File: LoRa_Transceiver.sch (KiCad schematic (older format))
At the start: 10 parts

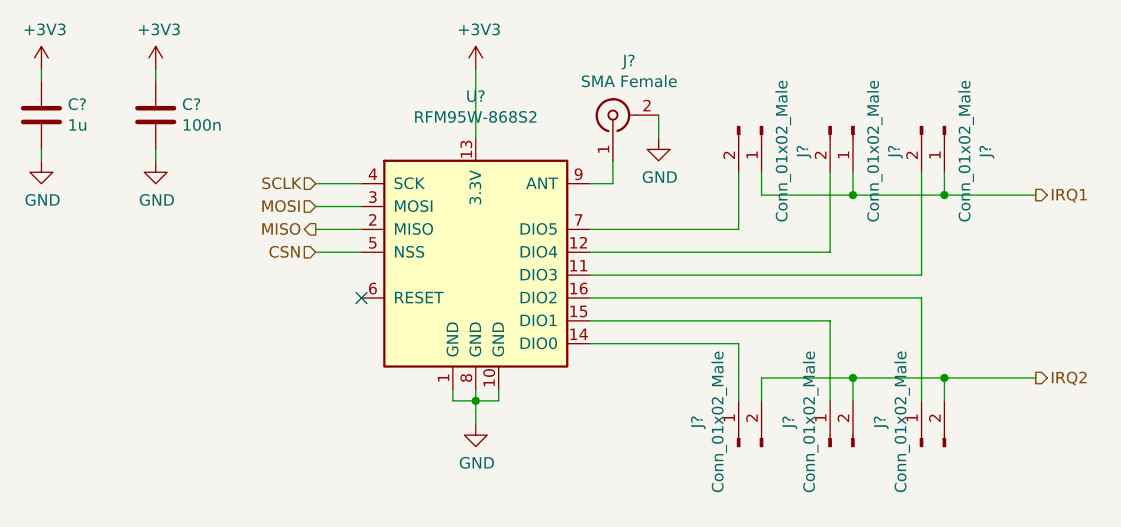
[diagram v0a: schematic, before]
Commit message: Change BME280 out for connector
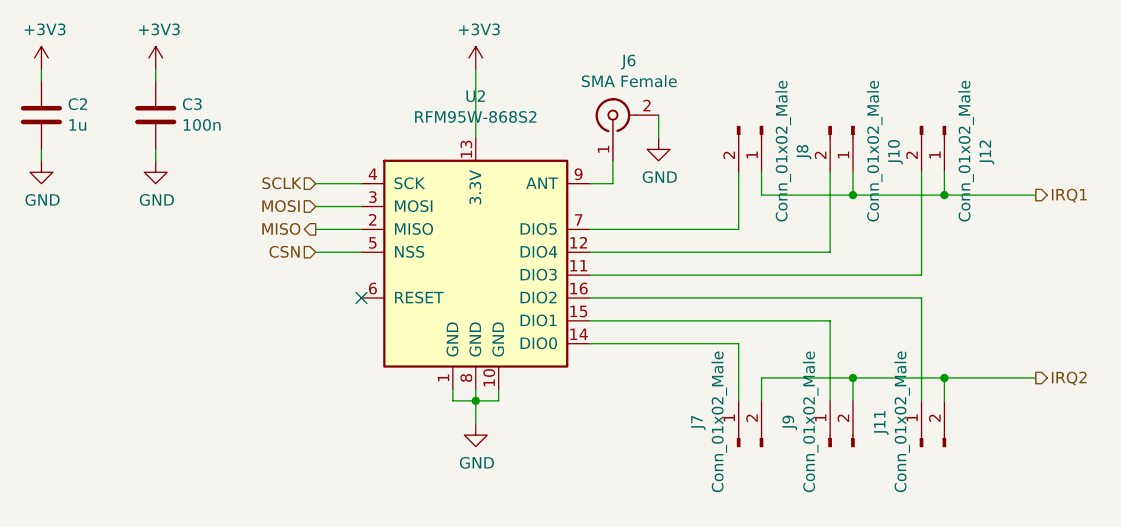
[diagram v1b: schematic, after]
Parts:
- gave numbers to parts that had none: 10
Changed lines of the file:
@@
 $EndDescr
 $Comp
-L RF_Module:RFM95W-868S2 U?
+L RF_Module:RFM95W-868S2 U2
 U 1 1 60A66EAC
 P 4400 3900
-F 0 "U?" H 4400 4581 50  0000 C CNN
+F 0 "U2" H 4400 4581 50  0000 C CNN
 F 1 "RFM95W-868S2" H 4400 4490 50  0000 C CNN
 F 2 "" H 1100 5550 50  0001 C CNN
@@
 CSN
 $Comp
-L power:+3V3 #PWR?
+L power:+3V3 #PWR022
 U 1 1 60A68377
 P 4400 3100
-F 0 "#PWR?" H 4400 2950 50  0001 C CNN
+F 0 "#PWR022" H 4400 2950 50  0001 C CNN
 F 1 "+3V3" H 4415 3273 50  0000 C CNN
 F 2 "" H 4400 3100 50  0001 C CNN
@@
 $EndComp
 $Comp
-L power:GND #PWR?
+L power:GND #PWR023
 U 1 1 60A684F7
 P 4400 4650
-F 0 "#PWR?" H 4400 4400 50  0001 C CNN
+F 0 "#PWR023" H 4400 4400 50  0001 C CNN
 F 1 "GND" H 4405 4477 50  0000 C CNN
 F 2 "" H 4400 4650 50  0001 C CNN
@@
 	5000 3600 5000 3500
 $Comp
-L Connector:Conn_01x02_Male J?
+L Connector:Conn_01x02_Male J8
 U 1 1 60A6BDC1
 P 5650 3350
-F 0 "J?" H 5758 3531 50  0000 C CNN
+F 0 "J8" H 5758 3531 50  0000 C CNN
 F 1 "Conn_01x02_Male" H 5758 3440 50  0000 C CNN
 F 2 "" H 5650 3350 50  0001 C CNN
@@
 $EndComp
 $Comp
-L Connector:Conn_01x02_Male J?
+L Connector:Conn_01x02_Male J10
 U 1 1 60A6C78E
 P 6050 3350
-F 0 "J?" H 6158 3531 50  0000 C CNN
+F 0 "J10" H 6158 3531 50  0000 C CNN
 F 1 "Conn_01x02_Male" H 6158 3440 50  0000 C CNN
 F 2 "" H 6050 3350 50  0001 C CNN
@@
 $EndComp
 $Comp
-L Connector:Conn_01x02_Male J?
+L Connector:Conn_01x02_Male J7
 U 1 1 60A6C92B
 P 5550 4750
-F 0 "J?" H 5658 4931 50  0000 C CNN
+F 0 "J7" H 5658 4931 50  0000 C CNN
 F 1 "Conn_01x02_Male" H 5658 4840 50  0000 C CNN
 F 2 "" H 5550 4750 50  0001 C CNN
@@
 $EndComp
 $Comp
-L Connector:Conn_01x02_Male J?
+L Connector:Conn_01x02_Male J9
 U 1 1 60A6CADE
 P 5950 4750
-F 0 "J?" H 6058 4931 50  0000 C CNN
+F 0 "J9" H 6058 4931 50  0000 C CNN
 F 1 "Conn_01x02_Male" H 6058 4840 50  0000 C CNN
 F 2 "" H 5950 4750 50  0001 C CNN
@@
 $EndComp
 $Comp
-L Connector:Conn_01x02_Male J?
+L Connector:Conn_01x02_Male J12
 U 1 1 60A6CCA7
 P 6450 3350
-F 0 "J?" H 6558 3531 50  0000 C CNN
+F 0 "J12" H 6558 3531 50  0000 C CNN
 F 1 "Conn_01x02_Male" H 6558 3440 50  0000 C CNN
 F 2 "" H 6450 3350 50  0001 C CNN
@@
 $EndComp
 $Comp
-L Connector:Conn_01x02_Male J?
+L Connector:Conn_01x02_Male J11
 U 1 1 60A6CE81
 P 6350 4750
-F 0 "J?" H 6458 4931 50  0000 C CNN
+F 0 "J11" H 6458 4931 50  0000 C CNN
 F 1 "Conn_01x02_Male" H 6458 4840 50  0000 C CNN
 F 2 "" H 6350 4750 50  0001 C CNN
@@
 	4900 4200 5950 4200
 $Comp
-L power:+3V3 #PWR?
+L power:+3V3 #PWR020
 U 1 1 60A81EA0
 P 3000 3100
-F 0 "#PWR?" H 3000 2950 50  0001 C CNN
+F 0 "#PWR020" H 3000 2950 50  0001 C CNN
 F 1 "+3V3" H 3015 3273 50  0000 C CNN
 F 2 "" H 3000 3100 50  0001 C CNN
@@
 $EndComp
 $Comp
-L power:GND #PWR?
+L power:GND #PWR021
 U 1 1 60A83B85
 P 3000 3500
-F 0 "#PWR?" H 3000 3250 50  0001 C CNN
+F 0 "#PWR021" H 3000 3250 50  0001 C CNN
 F 1 "GND" H 3005 3327 50  0000 C CNN
 F 2 "" H 3000 3500 50  0001 C CNN
@@
 $EndComp
 $Comp
-L Device:C C?
+L Device:C C3
 U 1 1 60A845BF
 P 3000 3300
-F 0 "C?" H 3115 3346 50  0000 L CNN
+F 0 "C3" H 3115 3346 50  0000 L CNN
 F 1 "100n" H 3115 3255 50  0000 L CNN
 F 2 "" H 3038 3150 50  0001 C CNN
@@
 	3000 3150 3000 3100
 $Comp
-L power:GND #PWR?
+L power:GND #PWR019
 U 1 1 60A85D82
 P 2500 3500
-F 0 "#PWR?" H 2500 3250 50  0001 C CNN
+F 0 "#PWR019" H 2500 3250 50  0001 C CNN
 F 1 "GND" H 2505 3327 50  0000 C CNN
 F 2 "" H 2500 3500 50  0001 C CNN
@@
 $EndComp
 $Comp
-L power:+3V3 #PWR?
+L power:+3V3 #PWR018
 U 1 1 60A86C18
 P 2500 3100
-F 0 "#PWR?" H 2500 2950 50  0001 C CNN
+F 0 "#PWR018" H 2500 2950 50  0001 C CNN
 F 1 "+3V3" H 2515 3273 50  0000 C CNN
 F 2 "" H 2500 3100 50  0001 C CNN
@@
 $EndComp
 $Comp
-L Device:C C?
+L Device:C C2
 U 1 1 60A882A8
 P 2500 3300
-F 0 "C?" H 2615 3346 50  0000 L CNN
+F 0 "C2" H 2615 3346 50  0000 L CNN
 F 1 "1u" H 2615 3255 50  0000 L CNN
 F 2 "" H 2538 3150 50  0001 C CNN
@@
 	2500 3150 2500 3100
 $Comp
-L Connector:Conn_Coaxial J?
+L Connector:Conn_Coaxial J6
 U 1 1 60A7FEF3
 P 5000 3300
-F 0 "J?" V 5237 3229 50  0000 C CNN
+F 0 "J6" V 5237 3229 50  0000 C CNN
 F 1 "SMA Female" V 5146 3229 50  0000 C CNN
 F 2 "" H 5000 3300 50  0001 C CNN
@@
 $EndComp
 $Comp
-L power:GND #PWR?
+L power:GND #PWR024
 U 1 1 60A8218B
 P 5200 3400
-F 0 "#PWR?" H 5200 3150 50  0001 C CNN
+F 0 "#PWR024" H 5200 3150 50  0001 C CNN
 F 1 "GND" H 5205 3227 50  0000 C CNN
 F 2 "" H 5200 3400 50  0001 C CNN

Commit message: Begin assigning footprints
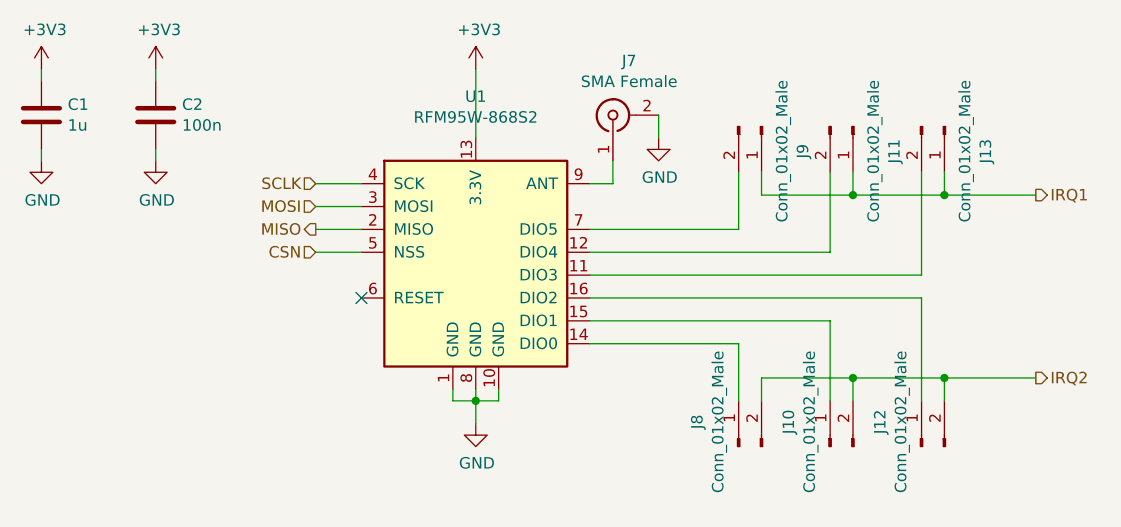
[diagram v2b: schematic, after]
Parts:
- C1: renamed from C2; footprint (none) -> Capacitor_SMD:C_0603_1608Metric; LCSC (none) -> C15849
- C2: renamed from C3; footprint (none) -> Capacitor_SMD:C_0603_1608Metric; LCSC (none) -> C14663
- J10: renamed from J9; footprint (none) -> Connector_PinHeader_2.54mm:PinHeader_1x02_P2.54mm_Vertical
- J11: renamed from J10; footprint (none) -> Connector_PinHeader_2.54mm:PinHeader_1x02_P2.54mm_Vertical
- J12: renamed from J11; footprint (none) -> Connector_PinHeader_2.54mm:PinHeader_1x02_P2.54mm_Vertical
- J13: renamed from J12; footprint (none) -> Connector_PinHeader_2.54mm:PinHeader_1x02_P2.54mm_Vertical
- J8: renamed from J7; footprint (none) -> Connector_PinHeader_2.54mm:PinHeader_1x02_P2.54mm_Vertical
- J9: renamed from J8; footprint (none) -> Connector_PinHeader_2.54mm:PinHeader_1x02_P2.54mm_Vertical
- renumbered J6 to J7, U2 to U1
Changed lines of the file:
@@
 $EndDescr
 $Comp
-L RF_Module:RFM95W-868S2 U2
+L RF_Module:RFM95W-868S2 U1
 U 1 1 60A66EAC
 P 4400 3900
-F 0 "U2" H 4400 4581 50  0000 C CNN
+F 0 "U1" H 4400 4581 50  0000 C CNN
 F 1 "RFM95W-868S2" H 4400 4490 50  0000 C CNN
 F 2 "" H 1100 5550 50  0001 C CNN
@@
 CSN
 $Comp
-L power:+3V3 #PWR022
+L power:+3V3 #PWR020
 U 1 1 60A68377
 P 4400 3100
-F 0 "#PWR022" H 4400 2950 50  0001 C CNN
+F 0 "#PWR020" H 4400 2950 50  0001 C CNN
 F 1 "+3V3" H 4415 3273 50  0000 C CNN
 F 2 "" H 4400 3100 50  0001 C CNN
@@
 $EndComp
 $Comp
-L power:GND #PWR023
+L power:GND #PWR021
 U 1 1 60A684F7
 P 4400 4650
-F 0 "#PWR023" H 4400 4400 50  0001 C CNN
+F 0 "#PWR021" H 4400 4400 50  0001 C CNN
 F 1 "GND" H 4405 4477 50  0000 C CNN
 F 2 "" H 4400 4650 50  0001 C CNN
@@
 	5000 3600 5000 3500
 $Comp
-L Connector:Conn_01x02_Male J8
+L Connector:Conn_01x02_Male J9
 U 1 1 60A6BDC1
 P 5650 3350
-F 0 "J8" H 5758 3531 50  0000 C CNN
+F 0 "J9" H 5758 3531 50  0000 C CNN
 F 1 "Conn_01x02_Male" H 5758 3440 50  0000 C CNN
-F 2 "" H 5650 3350 50  0001 C CNN
+F 2 "Connector_PinHeader_2.54mm:PinHeader_1x02_P2.54mm_Vertical" H 5650 3350 50  0001 C CNN
 F 3 "~" H 5650 3350 50  0001 C CNN
 	1    5650 3350
@@
 $EndComp
 $Comp
-L Connector:Conn_01x02_Male J10
+L Connector:Conn_01x02_Male J11
 U 1 1 60A6C78E
 P 6050 3350
-F 0 "J10" H 6158 3531 50  0000 C CNN
+F 0 "J11" H 6158 3531 50  0000 C CNN
 F 1 "Conn_01x02_Male" H 6158 3440 50  0000 C CNN
-F 2 "" H 6050 3350 50  0001 C CNN
+F 2 "Connector_PinHeader_2.54mm:PinHeader_1x02_P2.54mm_Vertical" H 6050 3350 50  0001 C CNN
 F 3 "~" H 6050 3350 50  0001 C CNN
 	1    6050 3350
@@
 $EndComp
 $Comp
-L Connector:Conn_01x02_Male J7
+L Connector:Conn_01x02_Male J8
 U 1 1 60A6C92B
 P 5550 4750
-F 0 "J7" H 5658 4931 50  0000 C CNN
+F 0 "J8" H 5658 4931 50  0000 C CNN
 F 1 "Conn_01x02_Male" H 5658 4840 50  0000 C CNN
-F 2 "" H 5550 4750 50  0001 C CNN
+F 2 "Connector_PinHeader_2.54mm:PinHeader_1x02_P2.54mm_Vertical" H 5550 4750 50  0001 C CNN
 F 3 "~" H 5550 4750 50  0001 C CNN
 	1    5550 4750
@@
 $EndComp
 $Comp
-L Connector:Conn_01x02_Male J9
+L Connector:Conn_01x02_Male J10
 U 1 1 60A6CADE
 P 5950 4750
-F 0 "J9" H 6058 4931 50  0000 C CNN
+F 0 "J10" H 6058 4931 50  0000 C CNN
 F 1 "Conn_01x02_Male" H 6058 4840 50  0000 C CNN
-F 2 "" H 5950 4750 50  0001 C CNN
+F 2 "Connector_PinHeader_2.54mm:PinHeader_1x02_P2.54mm_Vertical" H 5950 4750 50  0001 C CNN
 F 3 "~" H 5950 4750 50  0001 C CNN
 	1    5950 4750
@@
 $EndComp
 $Comp
-L Connector:Conn_01x02_Male J12
+L Connector:Conn_01x02_Male J13
 U 1 1 60A6CCA7
 P 6450 3350
-F 0 "J12" H 6558 3531 50  0000 C CNN
+F 0 "J13" H 6558 3531 50  0000 C CNN
 F 1 "Conn_01x02_Male" H 6558 3440 50  0000 C CNN
-F 2 "" H 6450 3350 50  0001 C CNN
+F 2 "Connector_PinHeader_2.54mm:PinHeader_1x02_P2.54mm_Vertical" H 6450 3350 50  0001 C CNN
 F 3 "~" H 6450 3350 50  0001 C CNN
 	1    6450 3350
@@
 $EndComp
 $Comp
-L Connector:Conn_01x02_Male J11
+L Connector:Conn_01x02_Male J12
 U 1 1 60A6CE81
 P 6350 4750
-F 0 "J11" H 6458 4931 50  0000 C CNN
+F 0 "J12" H 6458 4931 50  0000 C CNN
 F 1 "Conn_01x02_Male" H 6458 4840 50  0000 C CNN
-F 2 "" H 6350 4750 50  0001 C CNN
+F 2 "Connector_PinHeader_2.54mm:PinHeader_1x02_P2.54mm_Vertical" H 6350 4750 50  0001 C CNN
 F 3 "~" H 6350 4750 50  0001 C CNN
 	1    6350 4750
@@
 	4900 4200 5950 4200
 $Comp
-L power:+3V3 #PWR020
+L power:+3V3 #PWR018
 U 1 1 60A81EA0
 P 3000 3100
-F 0 "#PWR020" H 3000 2950 50  0001 C CNN
+F 0 "#PWR018" H 3000 2950 50  0001 C CNN
 F 1 "+3V3" H 3015 3273 50  0000 C CNN
 F 2 "" H 3000 3100 50  0001 C CNN
@@
 $EndComp
 $Comp
-L power:GND #PWR021
+L power:GND #PWR019
 U 1 1 60A83B85
 P 3000 3500
-F 0 "#PWR021" H 3000 3250 50  0001 C CNN
+F 0 "#PWR019" H 3000 3250 50  0001 C CNN
 F 1 "GND" H 3005 3327 50  0000 C CNN
 F 2 "" H 3000 3500 50  0001 C CNN
@@
 $EndComp
 $Comp
-L Device:C C3
+L Device:C C2
 U 1 1 60A845BF
 P 3000 3300
-F 0 "C3" H 3115 3346 50  0000 L CNN
+F 0 "C2" H 3115 3346 50  0000 L CNN
 F 1 "100n" H 3115 3255 50  0000 L CNN
-F 2 "" H 3038 3150 50  0001 C CNN
+F 2 "Capacitor_SMD:C_0603_1608Metric" H 3038 3150 50  0001 C CNN
 F 3 "~" H 3000 3300 50  0001 C CNN
+F 4 "C14663" H 3000 3300 50  0001 C CNN "LCSC"
 	1    3000 3300
 	1    0    0    -1
@@
 	3000 3150 3000 3100
 $Comp
-L power:GND #PWR019
+L power:GND #PWR017
 U 1 1 60A85D82
 P 2500 3500
-F 0 "#PWR019" H 2500 3250 50  0001 C CNN
+F 0 "#PWR017" H 2500 3250 50  0001 C CNN
 F 1 "GND" H 2505 3327 50  0000 C CNN
 F 2 "" H 2500 3500 50  0001 C CNN
@@
 $EndComp
 $Comp
-L power:+3V3 #PWR018
+L power:+3V3 #PWR016
 U 1 1 60A86C18
 P 2500 3100
-F 0 "#PWR018" H 2500 2950 50  0001 C CNN
+F 0 "#PWR016" H 2500 2950 50  0001 C CNN
 F 1 "+3V3" H 2515 3273 50  0000 C CNN
 F 2 "" H 2500 3100 50  0001 C CNN
@@
 $EndComp
 $Comp
-L Device:C C2
+L Device:C C1
 U 1 1 60A882A8
 P 2500 3300
-F 0 "C2" H 2615 3346 50  0000 L CNN
+F 0 "C1" H 2615 3346 50  0000 L CNN
 F 1 "1u" H 2615 3255 50  0000 L CNN
-F 2 "" H 2538 3150 50  0001 C CNN
+F 2 "Capacitor_SMD:C_0603_1608Metric" H 2538 3150 50  0001 C CNN
 F 3 "~" H 2500 3300 50  0001 C CNN
+F 4 "C15849" H 2500 3300 50  0001 C CNN "LCSC"
 	1    2500 3300
 	1    0    0    -1
@@
 	2500 3150 2500 3100
 $Comp
-L Connector:Conn_Coaxial J6
+L Connector:Conn_Coaxial J7
 U 1 1 60A7FEF3
 P 5000 3300
-F 0 "J6" V 5237 3229 50  0000 C CNN
+F 0 "J7" V 5237 3229 50  0000 C CNN
 F 1 "SMA Female" V 5146 3229 50  0000 C CNN
 F 2 "" H 5000 3300 50  0001 C CNN
@@
 $EndComp
 $Comp
-L power:GND #PWR024
+L power:GND #PWR022
 U 1 1 60A8218B
 P 5200 3400
-F 0 "#PWR024" H 5200 3150 50  0001 C CNN
+F 0 "#PWR022" H 5200 3150 50  0001 C CNN
 F 1 "GND" H 5205 3227 50  0000 C CNN
 F 2 "" H 5200 3400 50  0001 C CNN

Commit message: Finish attaching footprints for revision 1
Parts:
- J7: footprint (none) -> co2_sensor_node:TE_5-1814832-2_C482015
- U1: footprint (none) -> RF_Module:HOPERF_RFM9XW_SMD
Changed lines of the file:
@@
 F 0 "U1" H 4400 4581 50  0000 C CNN
 F 1 "RFM95W-868S2" H 4400 4490 50  0000 C CNN
-F 2 "" H 1100 5550 50  0001 C CNN
+F 2 "RF_Module:HOPERF_RFM9XW_SMD" H 1100 5550 50  0001 C CNN
 F 3 "https://www.hoperf.com/data/upload/portal/20181127/5bfcbea20e9ef.pdf" H 1100 5550 50  0001 C CNN
 	1    4400 3900
@@
 F 0 "J7" V 5237 3229 50  0000 C CNN
 F 1 "SMA Female" V 5146 3229 50  0000 C CNN
-F 2 "" H 5000 3300 50  0001 C CNN
+F 2 "co2_sensor_node:TE_5-1814832-2_C482015" H 5000 3300 50  0001 C CNN
 F 3 " ~" H 5000 3300 50  0001 C CNN
 	1    5000 3300

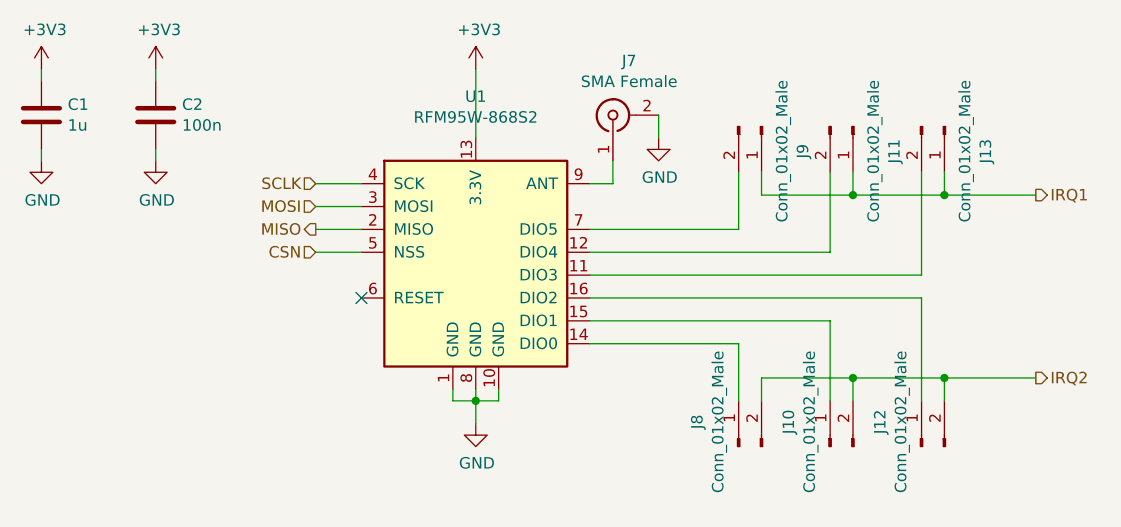
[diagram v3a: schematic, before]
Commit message: First cut at layout
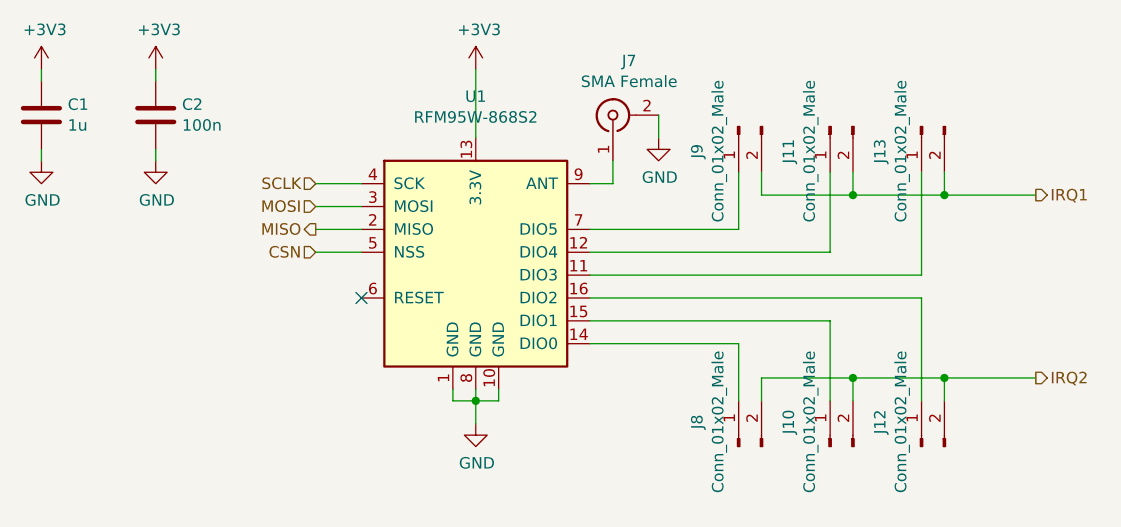
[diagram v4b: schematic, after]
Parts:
- J10, J11, J12, J13, J8, J9: footprint Connector_PinHeader_2.54mm:PinHeader_1x02_P2.54mm_Vertical -> Jumper:SolderJumper-2_P1.3mm_Open_TrianglePad1.0x1.5mm
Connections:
- net IRQ1: now also J11.2 (Pin_2), J13.2 (Pin_2), J9.2 (Pin_2); no longer J11.1 (Pin_1), J13.1 (Pin_1), J9.1 (Pin_1)
- net at U1.11 (DIO3): now also J13.1 (Pin_1); no longer J13.2 (Pin_2)
- net at U1.12 (DIO4): now also J11.1 (Pin_1); no longer J11.2 (Pin_2)
- net at U1.7 (DIO5): now also J9.1 (Pin_1); no longer J9.2 (Pin_2)
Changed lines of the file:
@@
 L Connector:Conn_01x02_Male J9
 U 1 1 60A6BDC1
-P 5650 3350
-F 0 "J9" H 5758 3531 50  0000 C CNN
-F 1 "Conn_01x02_Male" H 5758 3440 50  0000 C CNN
-F 2 "Connector_PinHeader_2.54mm:PinHeader_1x02_P2.54mm_Vertical" H 5650 3350 50  0001 C CNN
-F 3 "~" H 5650 3350 50  0001 C CNN
-	1    5650 3350
-	0    1    1    0
+P 5550 3350
+F 0 "J9" H 5658 3531 50  0000 C CNN
+F 1 "Conn_01x02_Male" H 5658 3440 50  0000 C CNN
+F 2 "Jumper:SolderJumper-2_P1.3mm_Open_TrianglePad1.0x1.5mm" H 5550 3350 50  0001 C CNN
+F 3 "~" H 5550 3350 50  0001 C CNN
+	1    5550 3350
+	0    -1   1    0
 $EndComp
 $Comp
 L Connector:Conn_01x02_Male J11
 U 1 1 60A6C78E
-P 6050 3350
-F 0 "J11" H 6158 3531 50  0000 C CNN
-F 1 "Conn_01x02_Male" H 6158 3440 50  0000 C CNN
-F 2 "Connector_PinHeader_2.54mm:PinHeader_1x02_P2.54mm_Vertical" H 6050 3350 50  0001 C CNN
-F 3 "~" H 6050 3350 50  0001 C CNN
-	1    6050 3350
-	0    1    1    0
+P 5950 3350
+F 0 "J11" H 6058 3531 50  0000 C CNN
+F 1 "Conn_01x02_Male" H 6058 3440 50  0000 C CNN
+F 2 "Jumper:SolderJumper-2_P1.3mm_Open_TrianglePad1.0x1.5mm" H 5950 3350 50  0001 C CNN
+F 3 "~" H 5950 3350 50  0001 C CNN
+	1    5950 3350
+	0    -1   1    0
 $EndComp
 $Comp
@@
 F 0 "J8" H 5658 4931 50  0000 C CNN
 F 1 "Conn_01x02_Male" H 5658 4840 50  0000 C CNN
-F 2 "Connector_PinHeader_2.54mm:PinHeader_1x02_P2.54mm_Vertical" H 5550 4750 50  0001 C CNN
+F 2 "Jumper:SolderJumper-2_P1.3mm_Open_TrianglePad1.0x1.5mm" H 5550 4750 50  0001 C CNN
 F 3 "~" H 5550 4750 50  0001 C CNN
 	1    5550 4750
@@
 F 0 "J10" H 6058 4931 50  0000 C CNN
 F 1 "Conn_01x02_Male" H 6058 4840 50  0000 C CNN
-F 2 "Connector_PinHeader_2.54mm:PinHeader_1x02_P2.54mm_Vertical" H 5950 4750 50  0001 C CNN
+F 2 "Jumper:SolderJumper-2_P1.3mm_Open_TrianglePad1.0x1.5mm" H 5950 4750 50  0001 C CNN
 F 3 "~" H 5950 4750 50  0001 C CNN
 	1    5950 4750
@@
 L Connector:Conn_01x02_Male J13
 U 1 1 60A6CCA7
-P 6450 3350
-F 0 "J13" H 6558 3531 50  0000 C CNN
-F 1 "Conn_01x02_Male" H 6558 3440 50  0000 C CNN
-F 2 "Connector_PinHeader_2.54mm:PinHeader_1x02_P2.54mm_Vertical" H 6450 3350 50  0001 C CNN
-F 3 "~" H 6450 3350 50  0001 C CNN
-	1    6450 3350
-	0    1    1    0
+P 6350 3350
+F 0 "J13" H 6458 3531 50  0000 C CNN
+F 1 "Conn_01x02_Male" H 6458 3440 50  0000 C CNN
+F 2 "Jumper:SolderJumper-2_P1.3mm_Open_TrianglePad1.0x1.5mm" H 6350 3350 50  0001 C CNN
+F 3 "~" H 6350 3350 50  0001 C CNN
+	1    6350 3350
+	0    -1   1    0
 $EndComp
 $Comp
@@
 F 0 "J12" H 6458 4931 50  0000 C CNN
 F 1 "Conn_01x02_Male" H 6458 4840 50  0000 C CNN
-F 2 "Connector_PinHeader_2.54mm:PinHeader_1x02_P2.54mm_Vertical" H 6350 4750 50  0001 C CNN
+F 2 "Jumper:SolderJumper-2_P1.3mm_Open_TrianglePad1.0x1.5mm" H 6350 4750 50  0001 C CNN
 F 3 "~" H 6350 4750 50  0001 C CNN
 	1    6350 4750

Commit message: Export fabrication files
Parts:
- J7: LCSC (none) -> C482015
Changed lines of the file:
@@
 F 2 "co2_sensor_node:TE_5-1814832-2_C482015" H 5000 3300 50  0001 C CNN
 F 3 " ~" H 5000 3300 50  0001 C CNN
+F 4 "C482015" H 5000 3300 50  0001 C CNN "LCSC"
 	1    5000 3300
 	0    -1   -1   0
